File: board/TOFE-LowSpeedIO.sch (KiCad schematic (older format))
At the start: 6 parts, among them U1 TOFE-8X, U7 24AA01/24LC01B

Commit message: Initial drop of TOFE LowSpeedIO Expansion Board.
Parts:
- removed C29: 0.1uF, ~, symbol C
- removed R15, R22: 10K, ~, symbol R
- removed U7: 24AA01/24LC01B, ~, symbol 24AA01/24LC01B
- added C1, C2: 22pF, ~, symbol C
- added C10, C3, C4: 0.1uF, ~, symbol C
- added C8, C9: 100uF, ~, symbol CP1
- added D1, D2, D3, D5, D6, D7: LED, ~, symbol LED
- added P1, P2, P3, P4: CONN_6X2, ~, symbol CONN_6X2
- added P5: CONN_2, ~, symbol CONN_2
- added P6: CONN_6, ~, symbol CONN_6
- added R1, R2, R3, R6, R7, R8, R9: 10K, ~, symbol R
- added R10: 100R, ~, symbol R
- added R4: 680R, ~, symbol RES_NET4
- added R5: 10K, ~, symbol RES_NET4
- added SW1, SW2, SW3, SW4: SW_PUSH, ~, symbol SW_PUSH
- added U2: AURD_COMM_SHIELD_ZERO_NEW, ~, symbol AURD_COMM_SHIELD_ZERO_NEW
- added U3: PIC18F14K50, ~, symbol PIC18F14K50
- added U5: 7805_NW, ~, symbol 7805_NW
- added X1: CRYSTAL, ~, symbol CRYSTAL
- added X2: USBMICRO, ~, symbol USBMICRO
- U1: value TOFE-8X -> TIMVIDEOS-PCIE-8X
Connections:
- net labels added: A0, A1, A2, A3, A4, A5, AREF, ATN, D0, D1, D10, D11, D12, D13, D14, D15, D2, D3, D4, D5, D6, D7, D8, D9, GPIO0_N, GPIO0_P, GPIO1_N, GPIO1_P, GPIO2_N, GPIO2_P, GPIO3_N, GPIO3_P, GPIO4_N, GPIO4_P, GPIO5_N, GPIO5_P, GPIO6_N, GPIO6_P, GPIO7_N, GPIO7_P, LED1, LED2, LED3, LED4, PGC, PGD, RESET, RX, SW1, SW2, SW3, SW4, TX, VCC5V, VPP
- wire segments 78 -> 348
- no-connect marks 1 -> 7
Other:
- note added: "12Mhz"
- note added: "ARDUINO ZERO SHIELD"
- note added: "EXPANSION CONNECTORS"
- note added: "FWUP"
- note added: "ICSP"
- note added: "LED"
- note added: "PIC18F14K50"
- note added: "POWER SUPPLY"
- note added: "PUSH BUTTON SWITCH"
- note added: "TOFE"
- note removed: "EEPROM"
- note removed: "TOFE-8x"

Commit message: Changes on 2015-11-03.
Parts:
- U1: value TIMVIDEOS-PCIE-8X -> TOFE-8X
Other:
- moved on the sheet: SW3
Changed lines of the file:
@@
 P 3600 4100
 F 0 "U1" H 3600 1250 60  0000 C CNN
-F 1 "TIMVIDEOS-PCIE-8X" H 2950 1250 60  0000 C CNN
+F 1 "TOFE-8X" H 2950 1250 60  0000 C CNN
 F 2 "~" H 2300 3800 60  0000 C CNN
 F 3 "~" H 2300 3800 60  0000 C CNN
@@
 L SW_PUSH SW3
 U 1 1 56164EC9
-P 13050 2150
-F 0 "SW3" H 13200 2260 50  0000 C CNN
-F 1 "SW_PUSH" H 13050 2070 50  0001 C CNN
-F 2 "~" H 13050 2150 60  0000 C CNN
-F 3 "~" H 13050 2150 60  0000 C CNN
-	1    13050 2150
+P 13000 2150
+F 0 "SW3" H 13150 2260 50  0000 C CNN
+F 1 "SW_PUSH" H 13000 2070 50  0001 C CNN
+F 2 "~" H 13000 2150 60  0000 C CNN
+F 3 "~" H 13000 2150 60  0000 C CNN
+	1    13000 2150
 	1    0    0    -1
 $EndComp
@@
 	2300 1700 2200 1700
 Wire Wire Line
-	2200 1700 2200 2000
-Wire Wire Line
-	2200 2000 2200 2800
-Wire Wire Line
-	2200 2800 2200 3100
-Wire Wire Line
-	2200 3100 2200 3300
-Wire Wire Line
-	2200 3300 2200 3700
-Wire Wire Line
-	2200 3700 2200 3800
-Wire Wire Line
-	2200 3800 2200 4100
-Wire Wire Line
-	2200 4100 2200 4200
-Wire Wire Line
-	2200 4200 2200 4500
-Wire Wire Line
-	2200 4500 2200 4900
-Wire Wire Line
-	2200 4900 2200 5200
-Wire Wire Line
-	2200 5200 2200 5300
-Wire Wire Line
-	2200 5300 2200 5600
-Wire Wire Line
-	2200 5600 2200 5700
-Wire Wire Line
-	2200 5700 2200 6000
-Wire Wire Line
-	2200 6000 2200 6100
-Wire Wire Line
-	2200 6100 2200 6400
-Wire Wire Line
-	2200 6400 2200 6600
-Wire Wire Line
-	2200 6600 2200 7150
+	2200 1700 2200 7150
 Wire Wire Line
 	2200 2000 2300 2000
@@
 	4000 1700 4100 1700
 Wire Wire Line
-	4100 1700 4100 2700
-Wire Wire Line
-	4100 2700 4100 3000
-Wire Wire Line
-	4100 3000 4100 3300
-Wire Wire Line
-	4100 3300 4100 3600
-Wire Wire Line
-	4100 3600 4100 3900
-Wire Wire Line
-	4100 3900 4100 4000
-Wire Wire Line
-	4100 4000 4100 4300
-Wire Wire Line
-	4100 4300 4100 4400
-Wire Wire Line
-	4100 4400 4100 4700
-Wire Wire Line
-	4100 4700 4100 5100
-Wire Wire Line
-	4100 5100 4100 5400
-Wire Wire Line
-	4100 5400 4100 5500
-Wire Wire Line
-	4100 5500 4100 5800
-Wire Wire Line
-	4100 5800 4100 5900
-Wire Wire Line
-	4100 5900 4100 6200
-Wire Wire Line
-	4100 6200 4100 6300
-Wire Wire Line
-	4100 6300 4100 6600
-Wire Wire Line
-	4100 6600 4100 7150
+	4100 1700 4100 7150
 Wire Wire Line
 	4100 3000 4000 3000
@@
 Connection ~ 4100 6300
 Wire Wire Line
-	4100 7150 3100 7150
-Wire Wire Line
-	3100 7150 2200 7150
+	4100 7150 2200 7150
 Connection ~ 2200 6600
 Connection ~ 4100 6600
@@
 	2100 2300 2300 2300
 Wire Wire Line
-	2100 1150 2100 2100
-Wire Wire Line
-	2100 2100 2100 2300
+	2100 1150 2100 2300
 Wire Wire Line
 	2100 2100 2300 2100
@@
 	4000 2200 4200 2200
 Wire Wire Line
-	4200 1150 4200 2200
-Wire Wire Line
-	4200 2200 4200 2300
+	4200 1150 4200 2300
 Wire Wire Line
 	4200 2300 4000 2300
 Wire Wire Line
-	2100 1150 3250 1150
-Wire Wire Line
-	3250 1150 4200 1150
+	2100 1150 4200 1150
 Connection ~ 4200 2200
 Connection ~ 2100 2100
@@
 	2250 1600 2300 1600
 Wire Wire Line
-	2250 1250 2250 1400
-Wire Wire Line
-	2250 1400 2250 1500
-Wire Wire Line
-	2250 1500 2250 1600
+	2250 1250 2250 1600
 Wire Wire Line
 	2250 1500 2300 1500
@@
 	4050 1600 4000 1600
 Wire Wire Line
-	4050 1250 4050 1500
-Wire Wire Line
-	4050 1500 4050 1600
+	4050 1250 4050 1600
 Wire Wire Line
 	4050 1500 4000 1500
 Wire Wire Line
-	2250 1250 3550 1250
-Wire Wire Line
-	3550 1250 4050 1250
+	2250 1250 4050 1250
 Connection ~ 4050 1500
 Connection ~ 2250 1400
@@
 	13900 7300 14000 7300
 Wire Wire Line
-	14000 7300 14000 7350
-Wire Wire Line
-	14000 7350 14000 7400
+	14000 7300 14000 7400
 Wire Wire Line
 	14000 7400 13900 7400
@@
 	11200 8100 10950 8100
 Wire Wire Line
-	8200 2150 8500 2150
-Wire Wire Line
-	8500 2150 8700 2150
-Wire Wire Line
-	8500 2550 9100 2550
-Wire Wire Line
-	9100 2550 9250 2550
-Wire Wire Line
-	9250 2550 9700 2550
-Wire Wire Line
-	9700 2550 10000 2550
+	8200 2150 8700 2150
+Wire Wire Line
+	8500 2550 10000 2550
 Wire Wire Line
 	9100 2550 9100 2450
@@
 	12150 2150 11850 2150
 Wire Wire Line
-	12650 2150 12750 2150
+	12650 2150 12700 2150
 Wire Wire Line
 	12750 3200 12800 3200
@@
 	12250 3600 11950 3600
 Wire Wire Line
-	9500 2150 9700 2150
-Wire Wire Line
-	9700 2150 10000 2150
-Wire Wire Line
-	10000 2150 10350 2150
+	9500 2150 10350 2150
 Connection ~ 9700 2150
 Connection ~ 10000 2150
@@
 	3700 9150 3800 9150
 Wire Wire Line
-	3700 8550 3700 8850
-Wire Wire Line
-	3700 8850 3700 9150
+	3700 8550 3700 9150
 Wire Wire Line
 	3800 8550 3700 8550
 Connection ~ 4300 9150
 Wire Wire Line
-	4550 9150 4300 9150
-Wire Wire Line
-	4300 9150 4200 9150
+	4550 9150 4200 9150
 Wire Wire Line
 	4550 8750 4550 9150
@@
 Connection ~ 4300 8550
 Wire Wire Line
-	4550 8550 4300 8550
-Wire Wire Line
-	4300 8550 4200 8550
+	4550 8550 4200 8550
 Wire Wire Line
 	4550 8650 4550 8550
@@
 	9300 8250 9300 8500
 Wire Wire Line
-	9250 8500 9300 8500
-Wire Wire Line
-	9300 8500 9550 8500
+	9250 8500 9550 8500
 Connection ~ 9300 8500
 Wire Wire Line
@@
 	13200 3200 13300 3200
 Wire Wire Line
-	13300 3200 13300 3400
-Wire Wire Line
-	13300 3400 13300 3600
-Wire Wire Line
-	13300 3600 13300 3800
+	13300 3200 13300 3800
 Wire Wire Line
 	13300 3400 13200 3400
@@
 Connection ~ 13300 3400
 Wire Wire Line
-	13200 3800 13300 3800
-Wire Wire Line
-	13300 3800 13500 3800
+	13200 3800 13500 3800
 Connection ~ 13300 3600
 Connection ~ 13300 3800
@@
 	13350 1750 13400 1750
 Wire Wire Line
-	13400 1750 13400 1950
-Wire Wire Line
-	13400 1950 13400 2150
-Wire Wire Line
-	13400 2150 13400 2350
+	13400 1750 13400 2350
 Wire Wire Line
 	13400 1950 13350 1950
 Wire Wire Line
-	13400 2150 13350 2150
+	13400 2150 13300 2150
 Connection ~ 13400 1950
 Wire Wire Line
-	13350 2350 13400 2350
-Wire Wire Line
-	13400 2350 13650 2350
+	13350 2350 13650 2350
 Connection ~ 13400 2150
 Connection ~ 13400 2350

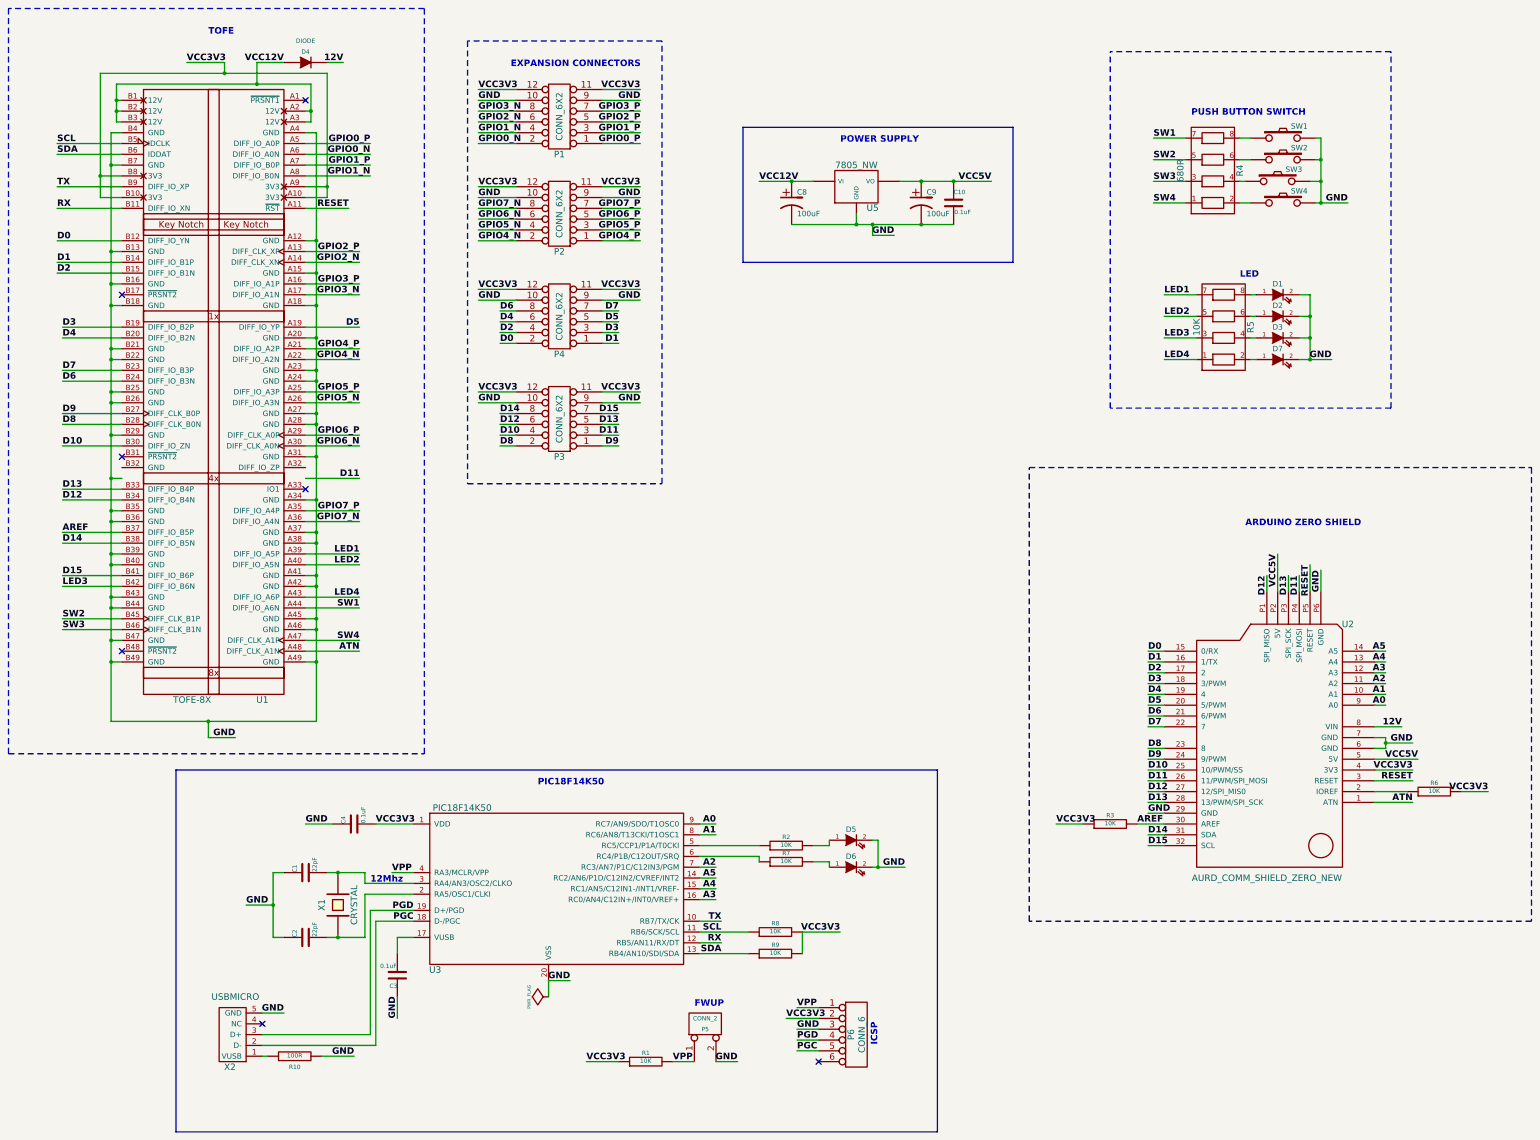
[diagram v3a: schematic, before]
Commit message: Mounting holes rearrangements.
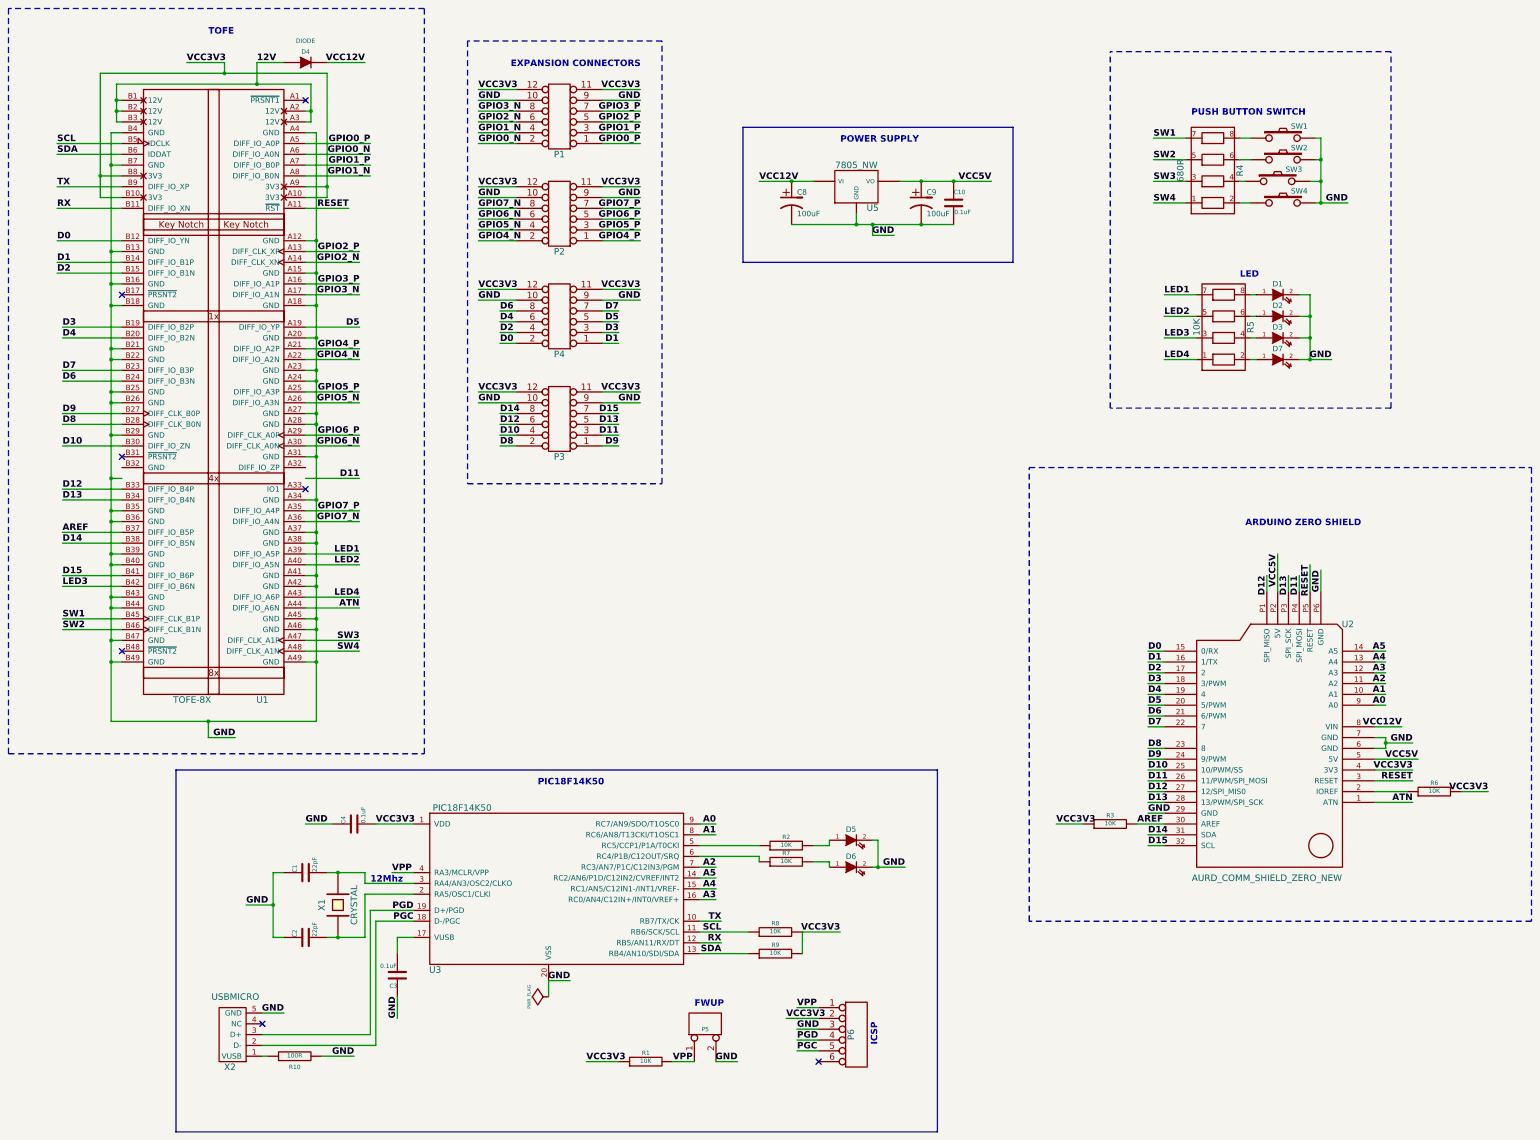
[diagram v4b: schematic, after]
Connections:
- net 12V: now also D4.1 (A), U1.A2 (12V), U1.A3 (12V), U1.B1 (12V), U1.B2 (12V), U1.B3 (12V); no longer D4.2 (K), U2.8 (VIN)
- net ATN: now also U1.A44 (DIFF_IO_A6N); no longer U1.A48 (DIFF_CLK_A1N)
- net D12: now also U1.B33 (DIFF_IO_B4P); no longer U1.B34 (DIFF_IO_B4N)
- net D13: now also U1.B34 (DIFF_IO_B4N); no longer U1.B33 (DIFF_IO_B4P)
- net SW1: now also U1.B45 (DIFF_CLK_B1P); no longer U1.A44 (DIFF_IO_A6N)
- net SW2: now also U1.B46 (DIFF_CLK_B1N); no longer U1.B45 (DIFF_CLK_B1P)
- net SW3: now also U1.A47 (DIFF_CLK_A1P); no longer U1.B46 (DIFF_CLK_B1N)
- net SW4: now also U1.A48 (DIFF_CLK_A1N); no longer U1.A47 (DIFF_CLK_A1P)
- net VCC12V: now also D4.2 (K), U2.8 (VIN); no longer D4.1 (A), U1.A2 (12V), U1.A3 (12V), U1.B1 (12V), U1.B2 (12V), U1.B3 (12V)
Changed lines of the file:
@@
 Sheet 1 1
 Title "TOFE Low Speed IO Module"
-Date "15 oct 2015"
+Date "2 nov 2015"
 Rev ""
 Comp "Numato Lab"
@@
 P 6350 1550
 F 0 "P1" H 6350 1900 60  0000 C CNN
-F 1 "CONN_6X2" V 6350 1550 60  0000 C CNN
+F 1 "CONN_6X2" V 6350 1550 60  0001 C CNN
 F 2 "~" H 6350 1550 60  0000 C CNN
 F 3 "~" H 6350 1550 60  0000 C CNN
@@
 P 6350 2450
 F 0 "P2" H 6350 2800 60  0000 C CNN
-F 1 "CONN_6X2" V 6350 2450 60  0000 C CNN
+F 1 "CONN_6X2" V 6350 2450 60  0001 C CNN
 F 2 "~" H 6350 2450 60  0000 C CNN
 F 3 "~" H 6350 2450 60  0000 C CNN
@@
 Text Label 13650 2350 2    60   ~ 12
 GND
-Text Label 3800 1050 2    60   ~ 12
+Text Label 4550 1050 2    60   ~ 12
 VCC12V
 Text Label 14250 7600 2    60   ~ 12
@@
 Text Label 4500 4900 2    60   ~ 12
 D11
+Text Label 1750 5000 0    60   ~ 12
+D12
 Text Label 1750 5100 0    60   ~ 12
-D12
-Text Label 1750 5000 0    60   ~ 12
 D13
 Text Label 1750 5500 0    60   ~ 12
@@
 Text Label 4500 5700 2    60   ~ 12
 LED2
-Text Label 4500 6100 2    60   ~ 12
+Text Label 1750 6200 0    60   ~ 12
 SW1
-Text Label 1750 6200 0    60   ~ 12
+Text Label 1750 6300 0    60   ~ 12
 SW2
 Text Label 14250 7350 2    60   ~ 12
@@
 P 6350 3400
 F 0 "P4" H 6350 3750 60  0000 C CNN
-F 1 "CONN_6X2" V 6350 3400 60  0000 C CNN
+F 1 "CONN_6X2" V 6350 3400 60  0001 C CNN
 F 2 "~" H 6350 3400 60  0000 C CNN
 F 3 "~" H 6350 3400 60  0000 C CNN
@@
 Text Label 1750 5400 0    60   ~ 12
 AREF
-Text Label 4500 6500 2    60   ~ 12
+Text Label 4500 6100 2    60   ~ 12
 ATN
 $Comp
@@
 Text Label 1750 5900 0    60   ~ 12
 LED3
-Text Label 1750 6300 0    60   ~ 12
+Text Label 4500 6400 2    60   ~ 12
 SW3
 $Comp
@@
 	1    0    0    -1
 $EndComp
-Text Label 14150 7200 2    60   ~ 12
-12V
 $Comp
 L CONN_6X2 P3
@@
 P 6350 4350
 F 0 "P3" H 6350 4700 60  0000 C CNN
-F 1 "CONN_6X2" V 6350 4350 60  0000 C CNN
+F 1 "CONN_6X2" V 6350 4350 60  0001 C CNN
 F 2 "~" H 6350 4350 60  0000 C CNN
 F 3 "~" H 6350 4350 60  0000 C CNN
@@
 Text Label 11800 8300 0    60   ~ 12
 D15
-Text Label 4350 1050 2    60   ~ 12
-12V
 Text Label 12900 5800 3    60   ~ 12
 D12
@@
 P 9100 10050
 F 0 "P6" V 9050 10050 60  0000 C CNN
-F 1 "CONN_6" V 9150 10050 60  0000 C CNN
+F 1 "CONN_6" V 9150 10050 60  0001 C CNN
 F 2 "~" H 9100 10050 60  0000 C CNN
 F 3 "~" H 9100 10050 60  0000 C CNN
@@
 P 7700 9950
 F 0 "P5" V 7650 9950 40  0000 C CNN
-F 1 "CONN_2" V 7750 9950 40  0000 C CNN
+F 1 "CONN_2" V 7750 9950 40  0001 C CNN
 F 2 "~" H 7700 9950 60  0000 C CNN
 F 3 "~" H 7700 9950 60  0000 C CNN
@@
 Text Label 11850 2350 0    60   ~ 12
 SW4
-Text Label 4500 6400 2    60   ~ 12
+Text Label 4500 6500 2    60   ~ 12
 SW4
 Text Label 4500 6000 2    60   ~ 12
@@
 	13900 7200 14150 7200
 Wire Wire Line
-	4200 1050 4350 1050
+	4200 1050 4550 1050
 Wire Wire Line
 	5950 2600 5600 2600
@@
 	4150 10250 4450 10250
 NoConn ~ 3600 9950
+Text Label 3550 1050 0    60   ~ 12
+12V
+Text Label 14150 7200 2    60   ~ 12
+VCC12V
 $EndSCHEMATC
